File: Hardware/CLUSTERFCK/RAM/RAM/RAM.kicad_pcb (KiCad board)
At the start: 4 copper layers, 142 x 62 mm, 41 parts, among them J1 Conn_02x10_Counter_Clockwise, J2 Conn_02x06_Counter_Clockwise, J3 Conn_02x08_Counter_Clockwise, J5 Conn_02x06_Counter_Clockwise, J6 Conn_02x08_Counter_Clockwise, J7 Conn_02x04_Odd_Even, J8 Conn_02x06_Odd_Even, U1 74LS245, U10 74HCT164, U11 74LS157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

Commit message: 0055 | 2h | Review RAM
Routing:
- net CLK: track 143.2 -> 134.0 mm
- net RAMOBUS11: track 126.4 -> 118.3 mm
- net RAMOBUS10: track 140.8 -> 132.9 mm, vias 6 -> 5
- net RAMOBUS9: track 144.5 -> 137.0 mm
- net RAMOBUS8: track 143.0 -> 135.6 mm
- net RAMDI: track 127.3 -> 121.7 mm
- net RAMOBUS12: track 118.2 -> 113.6 mm, vias 5 -> 3
- net RAMOBUS14: track 117.7 -> 113.4 mm
- net RAMOBUS5: track 134.9 -> 130.7 mm
- net DATA2: track 134.4 -> 130.3 mm
- net RAMOBUS13: track 116.3 -> 112.3 mm
- net RAMOBUS1: track 165.9 -> 161.9 mm, vias 8 -> 7
- net RAMAI: track 137.1 -> 133.5 mm
- net DATA6: track 140.0 -> 136.4 mm
- net /CLK_A: track 108.4 -> 104.9 mm
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
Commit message: 0066 | 6h | made holes in pcbs
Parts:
- added REF**: MountingHole_4.3mm_M4, MountingHole:MountingHole_4.3mm_M4, F.Cu at (45.3, 85.6)
- added REF**: MountingHole_4.3mm_M4, MountingHole:MountingHole_4.3mm_M4, F.Cu at (168.9, 83.0)
- added REF**: MountingHole_4.3mm_M4, MountingHole:MountingHole_4.3mm_M4, F.Cu at (168.9, 34.1)
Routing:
- net /CLK_A: track 104.9 -> 106.8 mm
- net Net-(J1-Pad2): track 105.8 -> 107.7 mm
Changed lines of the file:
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@@
     )
+  )
+  (footprint "MountingHole:MountingHole_4.3mm_M4" (layer "F.Cu")
+    (at 45.33 85.62)
+    (descr "Mounting Hole 4.3mm, no annular, M4")
+    (tags "mounting hole 4.3mm no annular m4")
+    (attr exclude_from_pos_files exclude_from_bom)
+    (fp_text reference "REF**" (at 0.15 -2.96) (layer "F.SilkS")
+      (effects (font (size 1 1) (thickness 0.15)))
+    )
+    (fp_text value "MountingHole_4.3mm_M4" (at 0 5.3) (layer "F.Fab")
+      (effects (font (size 1 1) (thickness 0.15)))
+    )
+    (fp_text user "${REFERENCE}" (at 0.3 0) (layer "F.Fab")
+      (effects (font (size 1 1) (thickness 0.15)))
+    )
+    (fp_circle (center 0 0) (end 4.3 0) (layer "Cmts.User") (width 0.15) (fill none))
+    (fp_circle (center 0 0) (end 4.55 0) (layer "F.CrtYd") (width 0.05) (fill none))
+    (pad "1" np_thru_hole circle (at 0 0) (size 4.3 4.3) (drill 4.3) (layers *.Cu *.Mask))
   )
   (footprint "Capacitor_SMD:C_0805_2012Metric_Pad1.15x1.40mm_HandSolder" (layer "F.Cu")
@@
     )
   )
+  (footprint "MountingHole:MountingHole_4.3mm_M4" (layer "F.Cu")
+    (at 168.95 83.03)
+    (descr "Mounting Hole 4.3mm, no annular, M4")
+    (tags "mounting hole 4.3mm no annular m4")
+    (attr exclude_from_pos_files exclude_from_bom)
+    (fp_text reference "REF**" (at 0.24 -3.35) (layer "F.SilkS")
+      (effects (font (size 1 1) (thickness 0.15)))
+    )
+    (fp_text value "MountingHole_4.3mm_M4" (at 0 5.3) (layer "F.Fab")
+      (effects (font (size 1 1) (thickness 0.15)))
+    )
+    (fp_text user "${REFERENCE}" (at 0.3 0) (layer "F.Fab")
+      (effects (font (size 1 1) (thickness 0.15)))
+    )
+    (fp_circle (center 0 0) (end 4.3 0) (layer "Cmts.User") (width 0.15) (fill none))
+    (fp_circle (center 0 0) (end 4.55 0) (layer "F.CrtYd") (width 0.05) (fill none))
+    (pad "1" np_thru_hole circle (at 0 0) (size 4.3 4.3) (drill 4.3) (layers *.Cu *.Mask))
+  )
   (footprint "Capacitor_SMD:C_0805_2012Metric_Pad1.15x1.40mm_HandSolder" (layer "F.Cu")
     (at 58.4 67.95 180)
@@
       (rotate (xyz 0 0 0))
     )
+  )
+  (footprint "MountingHole:MountingHole_4.3mm_M4" (layer "F.Cu")
+    (at 168.93 34.11)
+    (descr "Mounting Hole 4.3mm, no annular, M4")
+    (tags "mounting hole 4.3mm no annular m4")
+    (attr exclude_from_pos_files exclude_from_bom)
+    (fp_text reference "REF**" (at 0.4 3.45) (layer "F.SilkS")
+      (effects (font (size 1 1) (thickness 0.15)))
+    )
+    (fp_text value "MountingHole_4.3mm_M4" (at 0 5.3) (layer "F.Fab")
+      (effects (font (size 1 1) (thickness 0.15)))
+    )
+    (fp_text user "${REFERENCE}" (at 0.3 0) (layer "F.Fab")
+      (effects (font (size 1 1) (thickness 0.15)))
+    )
+    (fp_circle (center 0 0) (end 4.3 0) (layer "Cmts.User") (width 0.15) (fill none))
+    (fp_circle (center 0 0) (end 4.55 0) (layer "F.CrtYd") (width 0.05) (fill none))
+    (pad "1" np_thru_hole circle (at 0 0) (size 4.3 4.3) (drill 4.3) (layers *.Cu *.Mask))
   )
   (footprint "Package_SO:SOIC-14_3.9x8.7mm_P1.27mm" (layer "F.Cu")
@@
     (effects (font (size 1.5 1.5) (thickness 0.3)))
   )
-  (gr_text "RAM Module" (at 153.01 33.73) (layer "F.SilkS")
+  (gr_text "RAM Module" (at 147.09 33.32) (layer "F.SilkS")
     (effects (font (size 3 3) (thickness 0.5)))
   )
@@
   (segment (start 100.45 55.7) (end 100.45 57.1) (width 0.2) (layer "B.Cu") (net 17))
   (segment (start 90.645001 88.204999) (end 89.62 89.23) (width 0.2) (layer "B.Cu") (net 17))
+  (segment (start 55.59 84.05) (end 55.59 82.727798) (width 0.2) (layer "B.Cu") (net 17))
   (segment (start 100.47 63.9) (end 97.7 66.67) (width 0.2) (layer "B.Cu") (net 17))
   (segment (start 74.18 89.32) (end 74.14 89.36) (width 0.2) (layer "B.Cu") (net 17))
   (segment (start 94.282938 88.510736) (end 93.977201 88.204999) (width 0.2) (layer "B.Cu") (net 17))
   (segment (start 89.54 89.32) (end 74.18 89.32) (width 0.2) (layer "B.Cu") (net 17))
-  (segment (start 55.59 84.05) (end 37.91 84.05) (width 0.2) (layer "B.Cu") (net 17))
   (segment (start 93.977201 88.204999) (end 90.645001 88.204999) (width 0.2) (layer "B.Cu") (net 17))
   (segment (start 100.47 60.5) (end 100.47 63.9) (width 0.2) (layer "B.Cu") (net 17))
   (segment (start 100.7 60.27) (end 100.47 60.5) (width 0.2) (layer "B.Cu") (net 17))
-  (segment (start 37.91 84.05) (end 36.16 82.3) (width 0.2) (layer "B.Cu") (net 17))
   (segment (start 74.14 89.36) (end 60.75 89.36) (width 0.2) (layer "B.Cu") (net 17))
+  (segment (start 55.59 82.727798) (end 53.802202 80.94) (width 0.2) (layer "B.Cu") (net 17))
   (segment (start 94.282938 89.750942) (end 94.282938 88.510736) (width 0.2) (layer "B.Cu") (net 17))
+  (segment (start 53.802202 80.94) (end 50.44 80.94) (width 0.2) (layer "B.Cu") (net 17))
   (segment (start 100.7 57.55) (end 100.7 60.27) (width 0.2) (layer "B.Cu") (net 17))
+  (segment (start 50.44 80.94) (end 37.52 80.94) (width 0.2) (layer "B.Cu") (net 17))
   (segment (start 97.7 68.19) (end 96.64 69.25) (width 0.2) (layer "B.Cu") (net 17))
   (segment (start 97.7 66.67) (end 97.7 68.19) (width 0.2) (layer "B.Cu") (net 17))
@@
   (segment (start 94.761996 90.23) (end 94.282938 89.750942) (width 0.2) (layer "B.Cu") (net 17))
   (segment (start 89.62 89.24) (end 89.54 89.32) (width 0.2) (layer "B.Cu") (net 17))
+  (segment (start 37.52 80.94) (end 36.16 82.3) (width 0.2) (layer "B.Cu") (net 17))
   (segment (start 116.65 63.985) (end 116.375 63.71) (width 0.2) (layer "F.Cu") (net 18))
   (segment (start 106.665 63.9) (end 107.35 63.9) (width 0.2) (layer "F.Cu") (net 18))
@@
   (via (at 108.7625 65.3125) (size 0.43) (drill 0.3) (layers "F.Cu" "B.Cu") (net 18))
   (via (at 99.675001 89.665001) (size 0.43) (drill 0.3) (layers "F.Cu" "B.Cu") (net 18))
+  (segment (start 57.04 90.03) (end 47.45 80.44) (width 0.2) (layer "In1.Cu") (net 18))
   (segment (start 96.272797 89.665001) (end 99.675001 89.665001) (width 0.2) (layer "In1.Cu") (net 18))
-  (segment (start 39.1 82.3) (end 45.02 88.22) (width 0.2) (layer "In1.Cu") (net 18))
   (segment (start 38.7 82.3) (end 39.1 82.3) (width 0.2) (layer "In1.Cu") (net 18))
-  (segment (start 46.83 90.03) (end 95.907798 90.03) (width 0.2) (layer "In1.Cu") (net 18))
-  (segment (start 45.025001 88.225001) (end 46.83 90.03) (width 0.2) (layer "In1.Cu") (net 18))
+  (segment (start 41.52 80.44) (end 39.66 82.3) (width 0.2) (layer "In1.Cu") (net 18))
   (segment (start 95.907798 90.03) (end 96.272797 89.665001) (width 0.2) (layer "In1.Cu") (net 18))
+  (segment (start 39.66 82.3) (end 38.7 82.3) (width 0.2) (layer "In1.Cu") (net 18))
+  (segment (start 47.45 80.44) (end 41.52 80.44) (width 0.2) (layer "In1.Cu") (net 18))
+  (segment (start 57.04 90.03) (end 95.907798 90.03) (width 0.2) (layer "In1.Cu") (net 18))
   (segment (start 110.349999 81.790001) (end 111.5 80.64) (width 0.2) (layer "F.Cu") (net 19))
   (segment (start 111.5 86.84) (end 110.349999 85.689999) (width 0.2) (layer "F.Cu") (net 19))

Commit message: UNSTABLE PUSH! RAM NOT WIRED!
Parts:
- moved J2 31.8 mm to (92.4, 78.1)
- moved J5 31.8 mm to (92.4, 84.3)
- moved J3 28.5 mm to (125.4, 78.2)
- moved J6 28.5 mm to (125.4, 84.4)
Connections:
- J2 pad 1: (no net) -> MEMADDR10
- J2 pad 10: MEMADDR9 -> MEMADDR3
- J2 pad 11: MEMADDR10 -> (no net)
- J2 pad 12: MEMADDR11 -> MEMADDR1
- J2 pad 2: MEMADDR1 -> MEMADDR11
- J2 pad 3: MEMADDR2 -> MEMADDR8
- J2 pad 4: MEMADDR3 -> MEMADDR9
- J2 pad 5: MEMADDR4 -> MEMADDR6
- J2 pad 6: MEMADDR5 -> MEMADDR7
- J2 pad 7: MEMADDR6 -> MEMADDR4
- J2 pad 8: MEMADDR7 -> MEMADDR5
- J2 pad 9: MEMADDR8 -> MEMADDR2
- J3 pad 1: RAMOBUS0 -> RAMOBUS14
- J3 pad 10: RAMOBUS9 -> RAMOBUS7
- J3 pad 11: RAMOBUS10 -> RAMOBUS4
- J3 pad 12: RAMOBUS11 -> RAMOBUS5
- J3 pad 13: RAMOBUS12 -> RAMOBUS2
- J3 pad 14: RAMOBUS13 -> RAMOBUS3
- J3 pad 15: RAMOBUS14 -> RAMOBUS0
- J3 pad 16: RAMOBUS15 -> RAMOBUS1
- J3 pad 2: RAMOBUS1 -> RAMOBUS15
- J3 pad 3: RAMOBUS2 -> RAMOBUS12
- J3 pad 4: RAMOBUS3 -> RAMOBUS13
- J3 pad 5: RAMOBUS4 -> RAMOBUS10
- J3 pad 6: RAMOBUS5 -> RAMOBUS11
- J3 pad 7: RAMOBUS6 -> RAMOBUS8
- J3 pad 8: RAMOBUS7 -> RAMOBUS9
- J3 pad 9: RAMOBUS8 -> RAMOBUS6
- J5 pad 1: (no net) -> MEMADDR10
- J5 pad 10: MEMADDR9 -> MEMADDR3
- J5 pad 11: MEMADDR10 -> (no net)
- J5 pad 12: MEMADDR11 -> MEMADDR1
- J5 pad 2: MEMADDR1 -> MEMADDR11
- J5 pad 3: MEMADDR2 -> MEMADDR8
- J5 pad 4: MEMADDR3 -> MEMADDR9
- J5 pad 5: MEMADDR4 -> MEMADDR6
- J5 pad 6: MEMADDR5 -> MEMADDR7
- J5 pad 7: MEMADDR6 -> MEMADDR4
- J5 pad 8: MEMADDR7 -> MEMADDR5
- J5 pad 9: MEMADDR8 -> MEMADDR2
- J6 pad 1: RAMOBUS0 -> RAMOBUS14
- J6 pad 10: RAMOBUS9 -> RAMOBUS7
- J6 pad 11: RAMOBUS10 -> RAMOBUS4
- J6 pad 12: RAMOBUS11 -> RAMOBUS5
- J6 pad 13: RAMOBUS12 -> RAMOBUS2
- J6 pad 14: RAMOBUS13 -> RAMOBUS3
- J6 pad 15: RAMOBUS14 -> RAMOBUS0
- J6 pad 16: RAMOBUS15 -> RAMOBUS1
- J6 pad 2: RAMOBUS1 -> RAMOBUS15
- J6 pad 3: RAMOBUS2 -> RAMOBUS12
- J6 pad 4: RAMOBUS3 -> RAMOBUS13
- J6 pad 5: RAMOBUS4 -> RAMOBUS10
- J6 pad 6: RAMOBUS5 -> RAMOBUS11
- J6 pad 7: RAMOBUS6 -> RAMOBUS8
- J6 pad 8: RAMOBUS7 -> RAMOBUS9
- J6 pad 9: RAMOBUS8 -> RAMOBUS6
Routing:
- net +5V: track 358.4 -> 0.00 mm, vias 25 -> 0
- net RAMOBUS1: track 161.9 -> 0.00 mm, vias 7 -> 0
- net RAMOBUS0: track 154.1 -> 0.00 mm, vias 2 -> 0
- net READ: track 146.2 -> 0.00 mm, vias 1 -> 0
- net DATA7: track 144.5 -> 0.00 mm, vias 1 -> 0
- net DATA0: track 143.3 -> 0.00 mm, vias 1 -> 0
- net DATA1: track 142.5 -> 0.00 mm, vias 1 -> 0
- net DATA4: track 142.0 -> 0.00 mm, vias 2 -> 0
- net RAMOBUS2: track 140.5 -> 0.00 mm, vias 5 -> 0
- net RAMOBUS3: track 137.8 -> 0.00 mm, vias 8 -> 0
- net RAMOBUS6: track 137.4 -> 0.00 mm, vias 6 -> 0
- net DATA5: track 137.2 -> 0.00 mm, vias 2 -> 0
- net RAMOBUS9: track 137.0 -> 0.00 mm, vias 8 -> 0
- net DATA6: track 136.4 -> 0.00 mm, vias 2 -> 0
- net RAMOBUS4: track 136.4 -> 0.00 mm, vias 6 -> 0
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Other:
- board text added: "Leon Hellmich 2021"
- board text added: "RAM Module Rev 2"
- board text removed: "Leon Hellmich 2020"
- board text removed: "RAM Module"

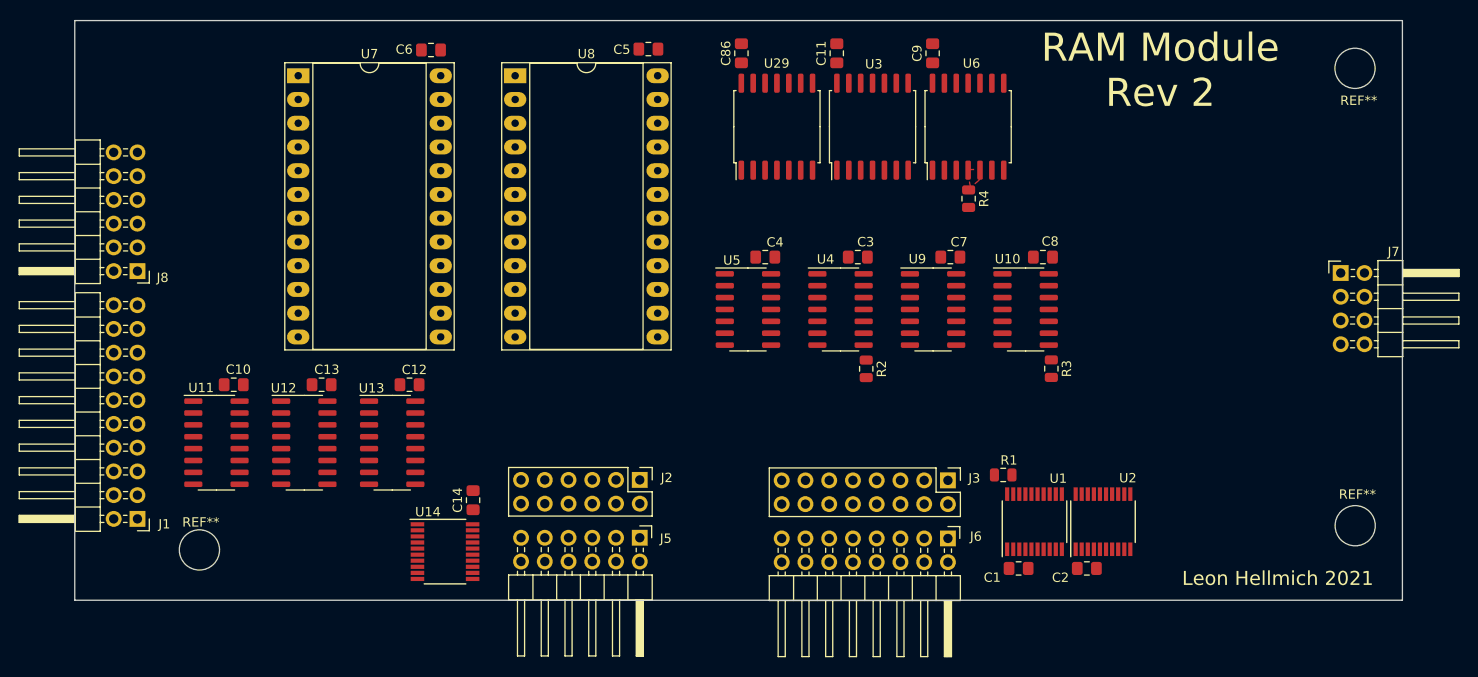
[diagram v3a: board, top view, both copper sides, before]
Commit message: 0070 | 6h | completely rerouted RAM
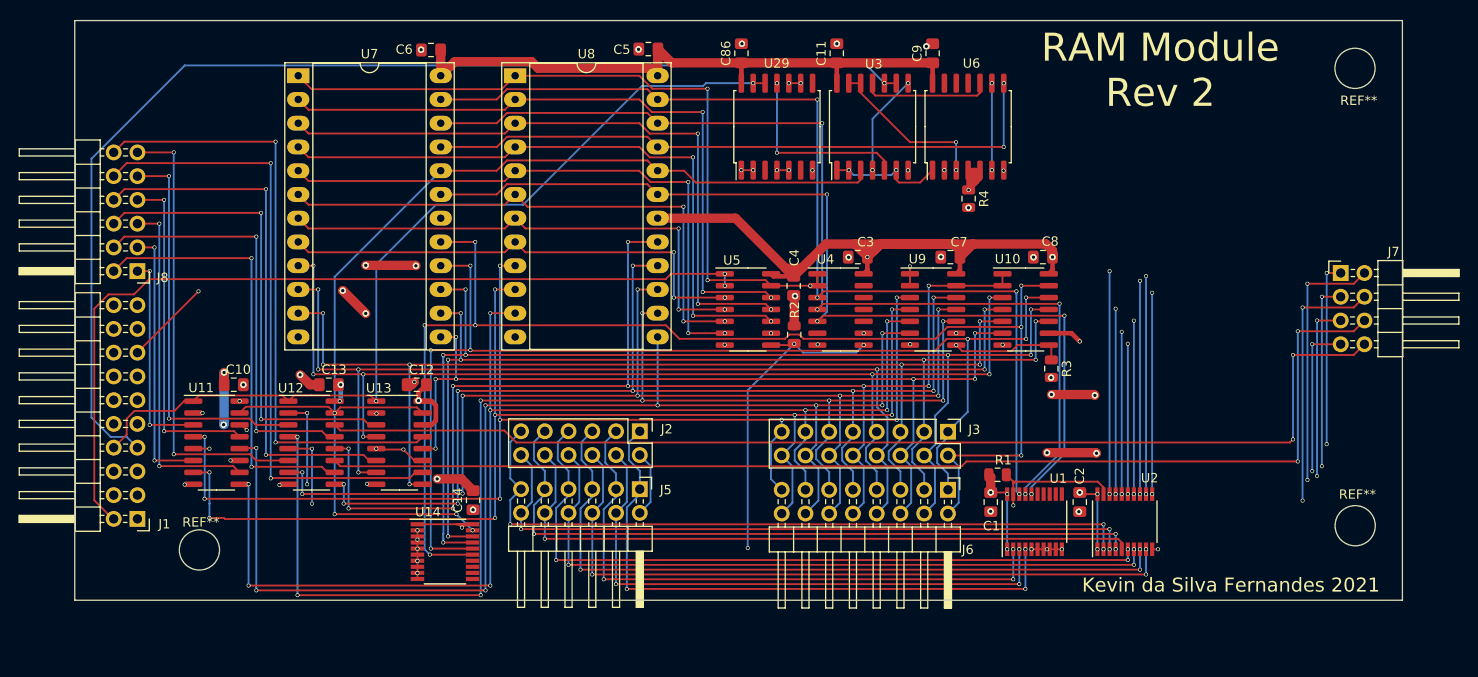
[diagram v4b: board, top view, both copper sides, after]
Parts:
- moved R2 8.53 mm to (109.0, 62.6), turned to 90 degrees
- moved C1 7.70 mm to (130.0, 80.5), turned to -90 degrees
- moved C2 7.14 mm to (139.5, 80.5), turned to -90 degrees
- moved J3 5.20 mm to (125.4, 73.0)
- moved J6 5.20 mm to (125.4, 79.2)
- moved J2 5.20 mm to (92.4, 72.9)
- moved J5 5.20 mm to (92.4, 79.1)
- moved C4 4.33 mm to (108.9, 57.4), turned to -90 degrees
- moved U2 2.33 mm to (144.3, 82.6)
- moved C13 0.77 mm to (59.2, 68.0)
- moved U12 0.77 mm to (57.3, 74.2)
- moved C12 0.77 mm to (68.6, 68.0)
- moved U13 0.77 mm to (66.7, 74.2)
- moved R1 0.60 mm to (130.7, 77.6)
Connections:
- J1 pad 13: no_connect_78 -> (no net)
- J1 pad 14: no_connect_79 -> (no net)
- J1 pad 17: no_connect_80 -> (no net)
- J1 pad 3: no_connect_81 -> (no net)
- J1 pad 4: no_connect_82 -> (no net)
- J1 pad 5: no_connect_83 -> (no net)
- J1 pad 6: no_connect_84 -> (no net)
- J2 pad 11: (no net) -> MEMADDR0
- J5 pad 11: (no net) -> MEMADDR0
- U1 pad 11: no_connect_85 -> (no net)
- U1 pad 12: no_connect_86 -> (no net)
- U1 pad 13: no_connect_87 -> (no net)
- U1 pad 14: no_connect_88 -> (no net)
- U1 pad 15: no_connect_89 -> (no net)
- U14 pad 11: no_connect_90 -> (no net)
- U14 pad 12: no_connect_91 -> (no net)
- U14 pad 13: no_connect_92 -> (no net)
- U14 pad 14: no_connect_93 -> (no net)
- U2 pad 2: (no net) -> MEMADDR0
- U29 pad 3: no_connect_94 -> (no net)
- U29 pad 6: no_connect_95 -> (no net)
- U29 pad 8: no_connect_96 -> (no net)
- U4 pad 10: no_connect_97 -> (no net)
- U4 pad 11: no_connect_98 -> (no net)
- U4 pad 12: no_connect_99 -> (no net)
- U4 pad 13: no_connect_100 -> (no net)
- U4 pad 6: no_connect_101 -> (no net)
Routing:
- net +5V: track 0.00 -> 364.6 mm, vias 0 -> 19
- net DATA4: track 0.00 -> 145.0 mm, vias 0 -> 4
- net DATA1: track 0.00 -> 143.8 mm, vias 0 -> 3
- net RAMOBUS15: track 0.00 -> 143.4 mm, vias 0 -> 7
- net DATA0: track 0.00 -> 143.0 mm, vias 0 -> 3
- net DATA5: track 0.00 -> 142.7 mm, vias 0 -> 4
- net BLOCK: track 0.00 -> 142.1 mm, vias 0 -> 1
- net RAMOBUS4: track 0.00 -> 139.3 mm, vias 0 -> 9
- net Net-(U2-Pad11): track 0.00 -> 138.0 mm, vias 0 -> 5
- net DATA2: track 0.00 -> 137.0 mm, vias 0 -> 3
- net RAMOBUS7: track 0.00 -> 136.6 mm, vias 0 -> 9
- net CLK: track 0.00 -> 136.4 mm, vias 0 -> 1
- net Net-(U2-Pad12): track 0.00 -> 135.9 mm, vias 0 -> 5
- net RAMOBUS3: track 0.00 -> 135.0 mm, vias 0 -> 8
- net Net-(U2-Pad13): track 0.00 -> 133.9 mm, vias 0 -> 5
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- removed copper zone on F.Cu, net READ
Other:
- board text added: "Kevin da Silva Fernandes 2021"
- board text removed: "Leon Hellmich 2021"
